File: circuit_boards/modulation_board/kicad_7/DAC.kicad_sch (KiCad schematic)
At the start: 4 parts

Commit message: Progress on circuit boards
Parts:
- added C305 (x2): 1u, Capacitor_SMD:C_0805_2012Metric, symbol Device:C
- added C305 (x8): 100n, Capacitor_SMD:C_0603_1608Metric, symbol Device:C
- added C507, C603, C604: 10u, Capacitor_SMD:C_0805_2012Metric, symbol Device:C
- added C605, C606, C607, C608: 1n, Capacitor_SMD:C_0603_1608Metric, symbol Device:C
- added R501: 2k7, Resistor_SMD:R_0603_1608Metric, symbol Device:R
- added R603, R604: 100k, Resistor_SMD:R_0603_1608Metric, symbol Device:R
- added R605, R607: 20k, Resistor_SMD:R_0603_1608Metric, symbol Device:R
- added R606, R609: 10k, Resistor_SMD:R_0603_1608Metric, symbol Device:R
- added R608, R611: 47k, Resistor_SMD:R_0603_1608Metric, symbol Device:R
- added R610: 68k, Resistor_SMD:R_0603_1608Metric, symbol Device:R
- added RV601, RV602: 5k, Potentiometer_THT:Potentiometer_Bourns_3296W_Vertical, symbol Device:R_Potentiometer_Trim
- added RV?: 10k, Potentiometer_THT:Potentiometer_Alpha_RD901F-40-00D_Single_Vertical, symbol Device:R_Potentiometer
- added TP1001: S&H_CV, TestPoint:TestPoint_Keystone_5000-5004_Miniature, symbol Connector:TestPoint
- added TP1001: PITCH_CV, TestPoint:TestPoint_Keystone_5000-5004_Miniature, symbol Connector:TestPoint
- added TP506: DAC_Vref, TestPoint:TestPoint_Keystone_5000-5004_Miniature, symbol Connector:TestPoint
- added U10: TL072, Package_SO:SOIC-8_3.9x4.9mm_P1.27mm, symbol Amplifier_Operational:TL072
- added U503: LM4040C-2.5, Package_TO_SOT_SMD:SOT-23, symbol Reference_Voltage:LM4040DBZ-2.5
- C602: renamed from C?; value C -> 1u; footprint (none) -> Capacitor_SMD:C_0805_2012Metric
- R602: renamed from R?; value R -> 10k; footprint (none) -> Resistor_SMD:R_0603_1608Metric
- U9: renamed from U?; value MCP48CxBx8 -> MCP48CVB28T-E/ML; footprint Package_DFN_QFN:QFN-20-1EP_4x4mm_P0.5mm_EP2.7x2.7mm_ThermalVias -> Package_DFN_QFN:QFN-20-1EP_4x4mm_P0.5mm_EP2.7x2.7mm
- gave numbers to parts that had none: 1
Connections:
- net MIDI_VCF_FREQ is gone; now on net MIDI_VCF_Q: U9.12 (VOUT_3)
- net GND: now also C305.2, C305.2, C305.2, C305.2, C305.2, C305.2, C305.2, C305.2, C305.2, C305.2, C507.2, C605.1, C606.1, R603.2, R604.2, RV601.2, RV601.3, RV602.2, RV602.3, RV?.1, U503.2 (A)
- net MIDI_MOD_WHEEL: now also U9.5 (VOUT_4), C305.1; no longer U9.11 (VOUT_5)
- net MIDI_VCF_Q: now also C305.1; no longer U9.5 (VOUT_4)
- net MOD_ENV: now also C305.1
- net PINK_NOISE: now also C603.2, R604.1; no longer U9.10 (VOUT_7)
- net PITCH_CV: now also C607.2, R610.2, TP1001.1, U10.1; no longer U8.1 (VOUTA)
- net S_AND_H_CV: now also C608.2, R611.2, TP1001.1, U10.7; no longer U8.2 (VOUTB)
- net VCA_ENV: now also C305.1
- net VCF_ENV: now also C305.1
- net WHITE_NOISE: now also C604.2, R603.1; no longer U9.6 (VOUT_6)
- net at U9.14 (VREF_1): now also U9.2 (VREF_0), C507.1, R501.2, TP506.1, U503.1 (K)
- net +3V3 renamed +3.3V
- net +3.3V: now also C305.1, C305.1, C305.1, C305.1
- new net: C603.1, U9.10 (VOUT_7)
- new net: C604.1, U9.11 (VOUT_5)
- new net: C305.1, RV?.3, U9.6 (VOUT_6)
- new net: C606.2, R609.2, U10.5 (+)
- new net: R607.1, RV602.1
- new net: C608.1, R607.2, R608.2, R611.1, U10.6 (-)
- new net: C607.1, R605.2, R610.1, U10.2 (-)
- new net: C605.2, R606.2, U10.3 (+)
- new net: R606.1, U8.1 (VOUTA)
- new net: R605.1, RV601.1
- new net: R609.1, U8.2 (VOUTB)
- new net +5V: R501.1, R608.1
- new net VOLUME_CV: RV?.2
- no-connect marks 1 -> 2
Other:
- note added: "MIDI 1V/oct trim"
- note added: "Master Volume"
- note added: "S&H 1V/oct trim"
- moved on the sheet: C602, R602, U8, U9

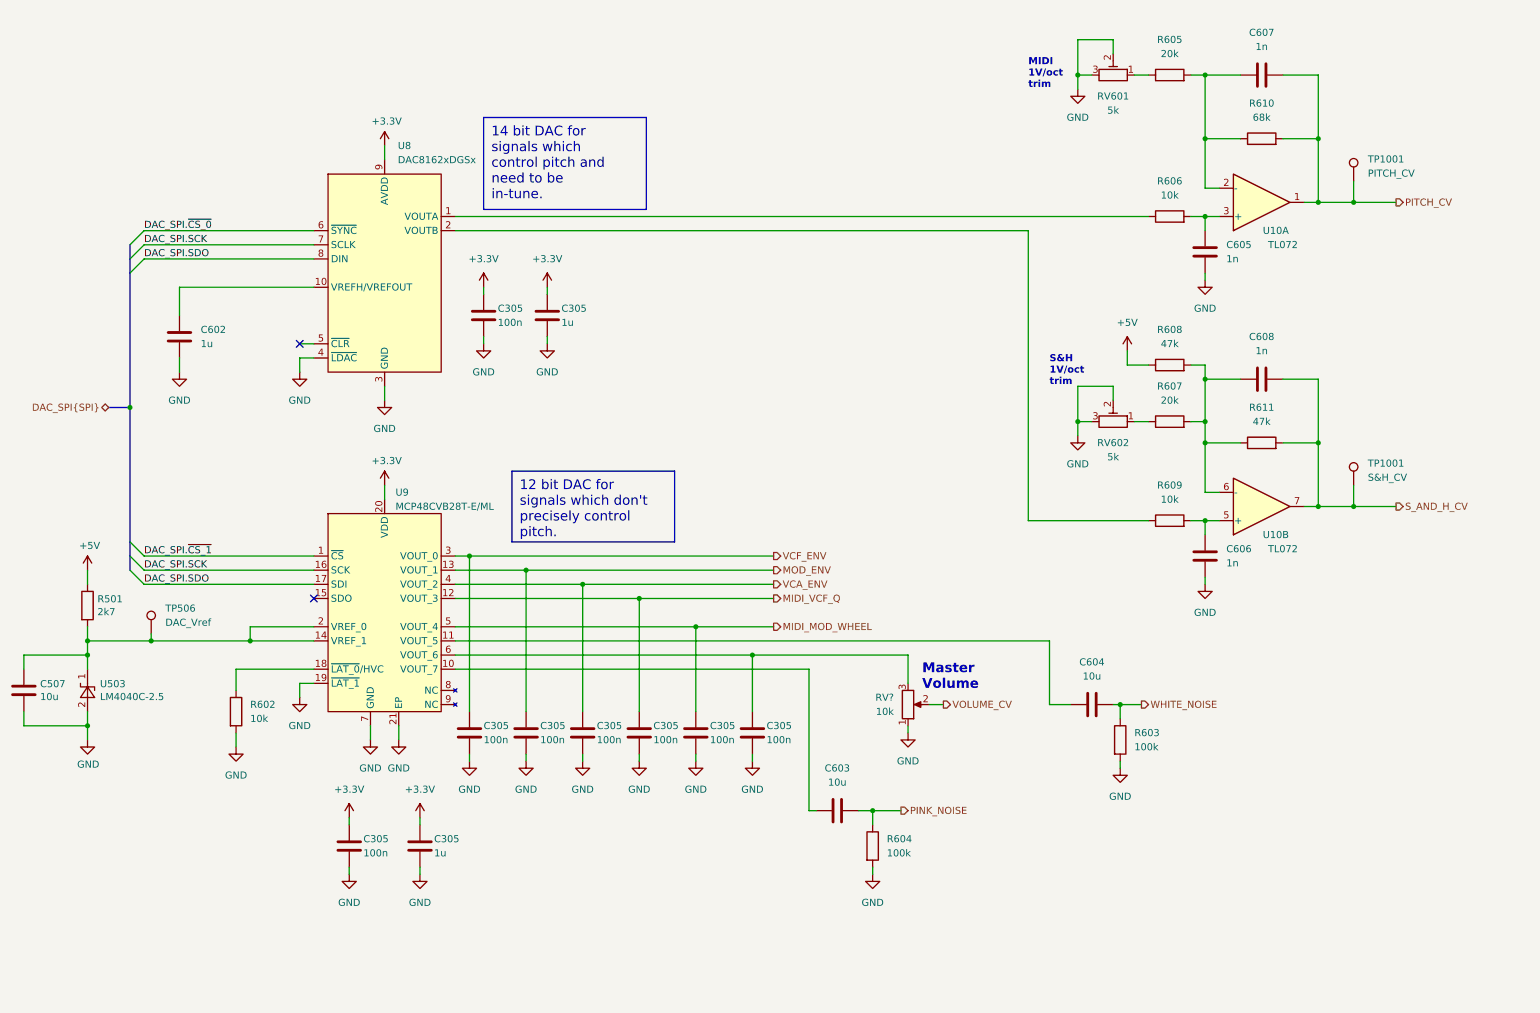
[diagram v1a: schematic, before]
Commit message: Tweaks to mod board, add debug pin
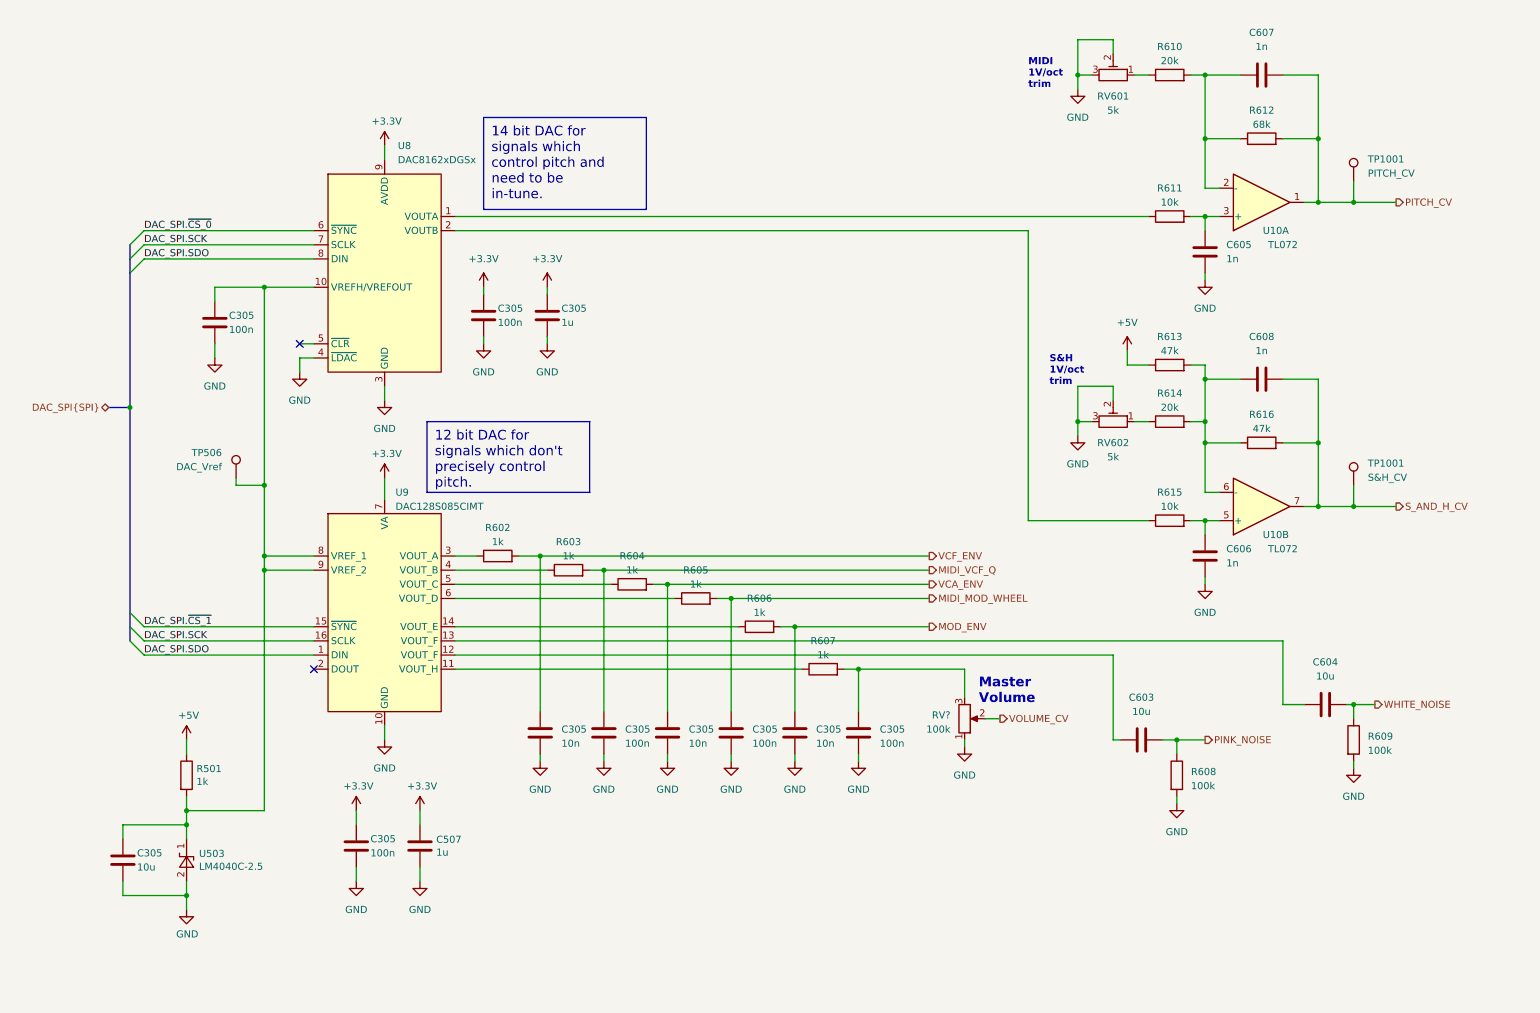
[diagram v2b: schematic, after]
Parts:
- removed C602: 1u, Capacitor_SMD:C_0805_2012Metric, symbol Device:C
- removed U9: MCP48CVB28T-E/ML, Package_DFN_QFN:QFN-20-1EP_4x4mm_P0.5mm_EP2.7x2.7mm, symbol custom_symbols:MCP48CVB28T-E/ML
- added C305: 100n, Capacitor_SMD:C_0603_1608Metric, symbol Device:C
- added R603, R604, R605, R606, R607: 1k, Resistor_SMD:R_0603_1608Metric, symbol Device:R
- added U9: DAC128S085CIMT, Package_SO:TSSOP-16_4.4x5mm_P0.65mm, symbol custom_symbols:DAC128S085CIMT
- C305: value 1u -> 10u
- C305: value 100n -> 10n
- C507: value 10u -> 1u
- R501: value 2k7 -> 1k
- R602: value 10k -> 1k
- RV?: value 10k -> 100k
- renumbered R604 to R608, R603 to R609, R605 to R610, R606 to R611, R610 to R612, R608 to R613, R607 to R614, R609 to R615, R611 to R616
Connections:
- net +3.3V: now also C507.1, U9.7 (VA); no longer C305.1
- net DAC_SPI.SCK: now also U9.16 (SCLK)
- net DAC_SPI.SDO: now also U9.1 (DIN)
- net DAC_SPI.~{CS_1}: now also U9.15 (~{SYNC})
- net GND: now also C305.2, U9.10 (GND); no longer R602.2
- net MIDI_MOD_WHEEL: now also C305.1, R605.2; no longer C305.1
- net MIDI_VCF_Q: now also C305.1, R603.2; no longer C305.1
- net MOD_ENV: now also C305.1, R606.2; no longer C305.1
- net VCA_ENV: now also R604.2
- net VCF_ENV: now also R602.2
- net at C603.1: now also U9.12 (VOUT_F)
- net at C604.1: now also U9.13 (VOUT_F)
- net at R501.2, TP506.1, U503.1 (K): now also C305.1, U8.10 (VREFH/VREFOUT), C305.1, U9.8 (VREF_1), U9.9 (VREF_2); no longer C507.1
- net at R602.1: now also U9.3 (VOUT_A)
- net at C305.1, RV?.3: now also R607.2
- new net: R603.1, U9.4 (VOUT_B)
- new net: R607.1, U9.11 (VOUT_H)
- new net: R604.1, U9.5 (VOUT_C)
- new net: R606.1, U9.14 (VOUT_E)
- new net: R605.1, U9.6 (VOUT_D)
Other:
- moved on the sheet: C305, C507, C603, C604, R608, R609, RV?, TP506

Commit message: Tweaks to mod board, debounce MODOSC toggle switch
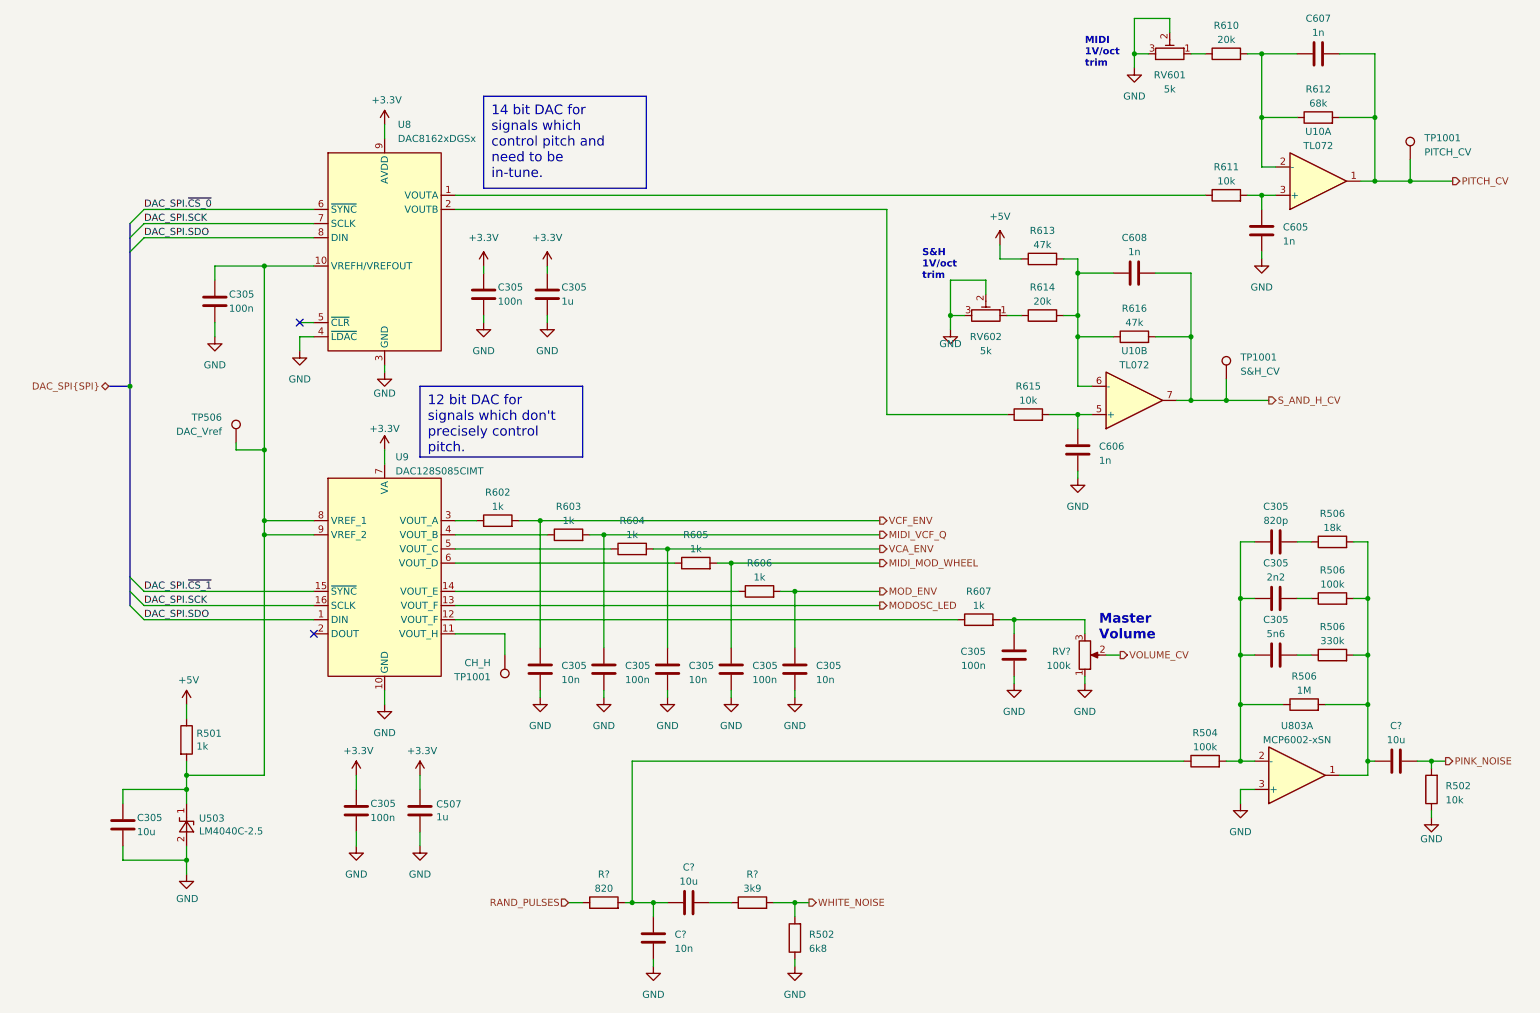
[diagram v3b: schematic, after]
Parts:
- removed C603, C604: 10u, Capacitor_SMD:C_0805_2012Metric, symbol Device:C
- removed R608, R609: 100k, Resistor_SMD:R_0603_1608Metric, symbol Device:R
- added C305: 2n2, Capacitor_SMD:C_0603_1608Metric, symbol Device:C
- added C305: 820p, Capacitor_SMD:C_0603_1608Metric, symbol Device:C
- added C305: 5n6, Capacitor_SMD:C_0603_1608Metric, symbol Device:C
- added C? (x2): 10u, Capacitor_SMD:C_0805_2012Metric, symbol Device:C
- added C?: 10n, Capacitor_SMD:C_0603_1608Metric, symbol Device:C
- added R502: 10k, Resistor_SMD:R_0603_1608Metric, symbol Device:R
- added R502: 6k8, Resistor_SMD:R_0603_1608Metric, symbol Device:R
- added R504, R506: 100k, Resistor_SMD:R_0603_1608Metric, symbol Device:R
- added R506: 1M, Resistor_SMD:R_0603_1608Metric, symbol Device:R
- added R506: 330k, Resistor_SMD:R_0603_1608Metric, symbol Device:R
- added R506: 18k, Resistor_SMD:R_0603_1608Metric, symbol Device:R
- added R?: 3k9, Resistor_SMD:R_0603_1608Metric, symbol Device:R
- added R?: 820, Resistor_SMD:R_0603_1608Metric, symbol Device:R
- added TP1001: CH_H, TestPoint:TestPoint_Keystone_5000-5004_Miniature, symbol Connector:TestPoint
- added U803: MCP6002-xSN, Package_SO:SOIC-8_3.9x4.9mm_P1.27mm, symbol Amplifier_Operational:MCP6002-xSN
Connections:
- net GND: now also C?.1, R502.1, R502.1, U803.3 (+)
- net PINK_NOISE: now also C?.2, R502.2
- net WHITE_NOISE: now also R502.2, R?.2
- net at U9.11 (VOUT_H): now also TP1001.1; no longer R607.1
- net MODOSC_LED: now reaches U9.13 (VOUT_F)
- net at U9.12 (VOUT_F): now also R607.1
- new net: C?.1, R506.2, R506.2, R506.2, R506.2, U803.1
- new net: C305.1, C305.1, C305.1, R504.2, R506.1, U803.2 (-)
- new net: C305.2, R506.1 (x3)
- new net: C?.1, C?.2, R504.1, R?.2
- new net: C?.2, R?.1
- new net RAND_PULSES: R?.1
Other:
- moved on the sheet: C305, C507, C605, C606, C607, C608, R501, R602, R603, R604, R605, R606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

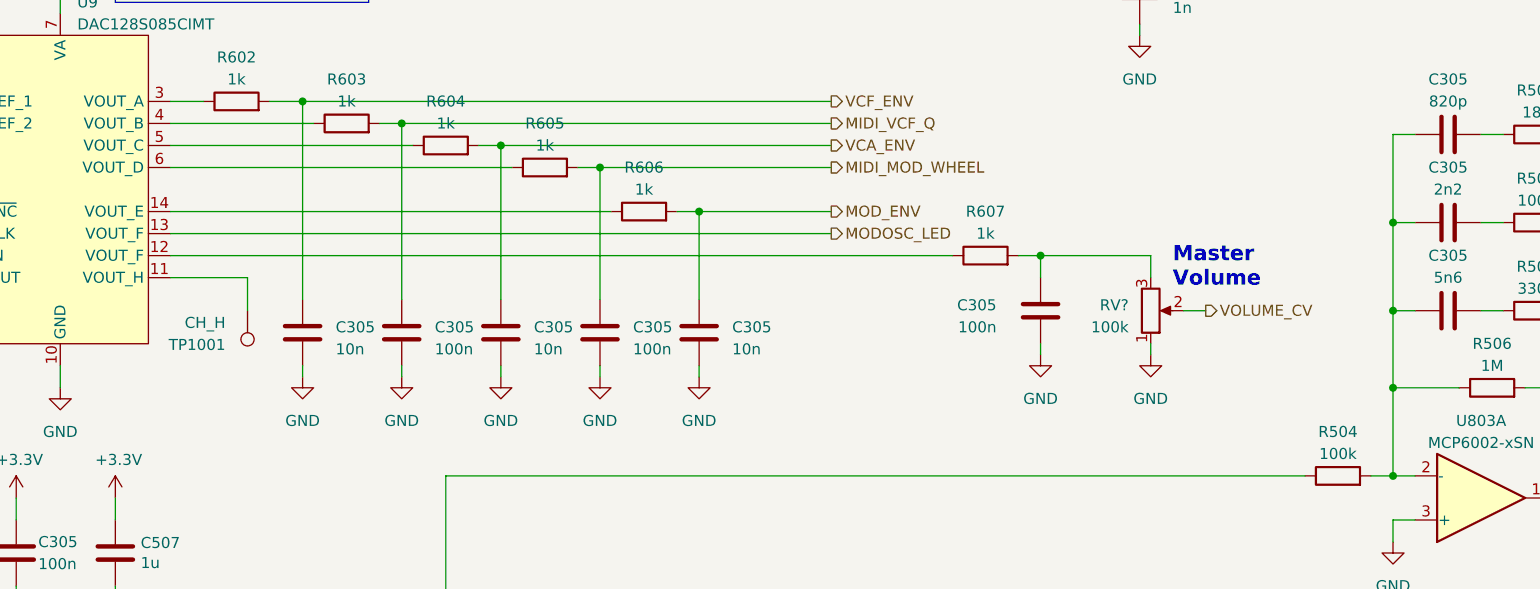
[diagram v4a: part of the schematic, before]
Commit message: Update PCBs, tweak vals, add VCF CV from DAC
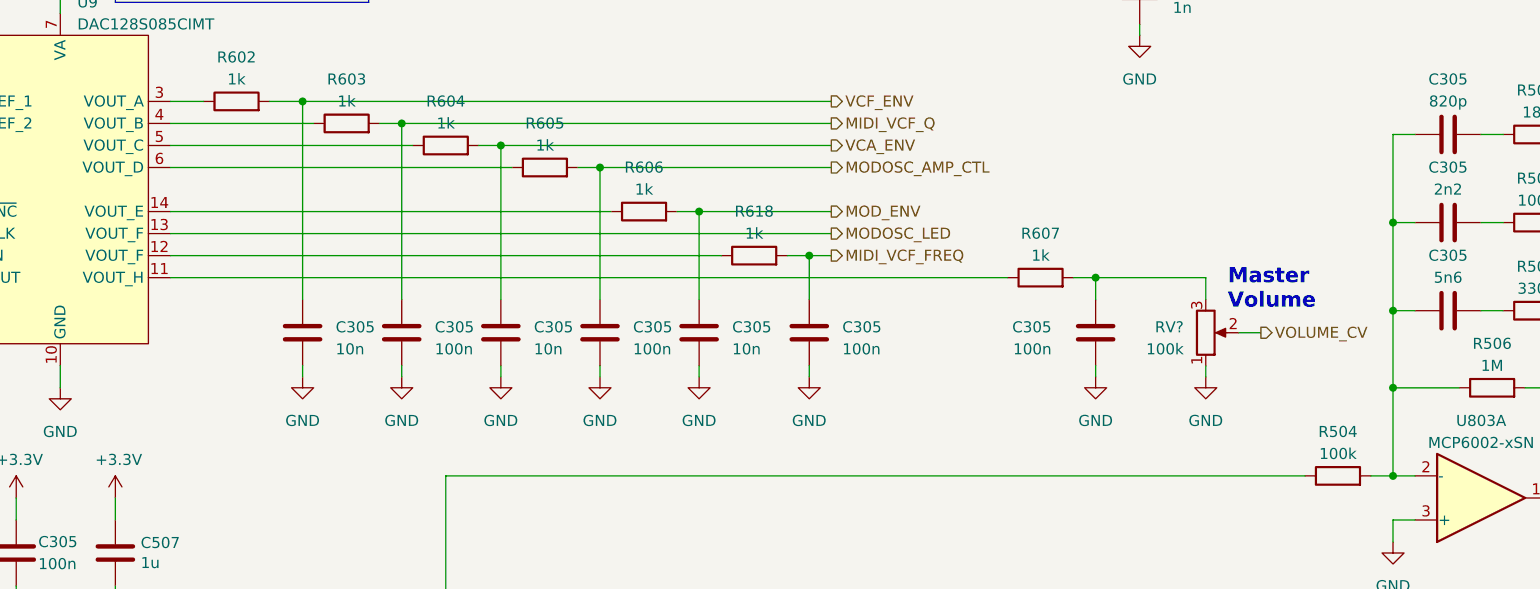
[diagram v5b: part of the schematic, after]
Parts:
- removed TP1001: CH_H, TestPoint:TestPoint_Keystone_5000-5004_Miniature, symbol Connector:TestPoint
- added C305: 100n, Capacitor_SMD:C_0603_1608Metric, symbol Device:C
- added R618: 1k, Resistor_SMD:R_0603_1608Metric, symbol Device:R
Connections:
- net GND: now also C305.2
- net at U9.11 (VOUT_H): now also R607.1
- net at U9.12 (VOUT_F): now also R618.1; no longer R607.1
- net MIDI_MOD_WHEEL renamed MODOSC_AMP_CTL
- new net MIDI_VCF_FREQ: C305.1, R618.2
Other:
- moved on the sheet: C305, R607, RV?
